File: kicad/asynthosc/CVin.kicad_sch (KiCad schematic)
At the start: 12 parts, among them J14 AudioJack3, SW11 SW_DIP_x04, U8 MCP6004

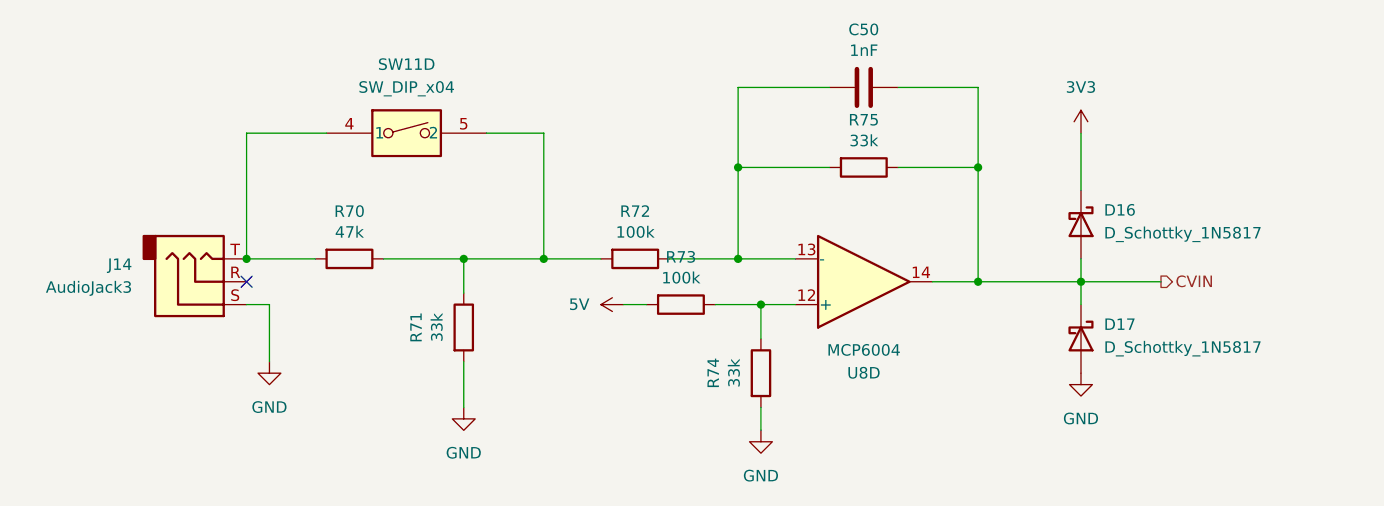
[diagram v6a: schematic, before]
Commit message: pcb: place and change some components for easier routing
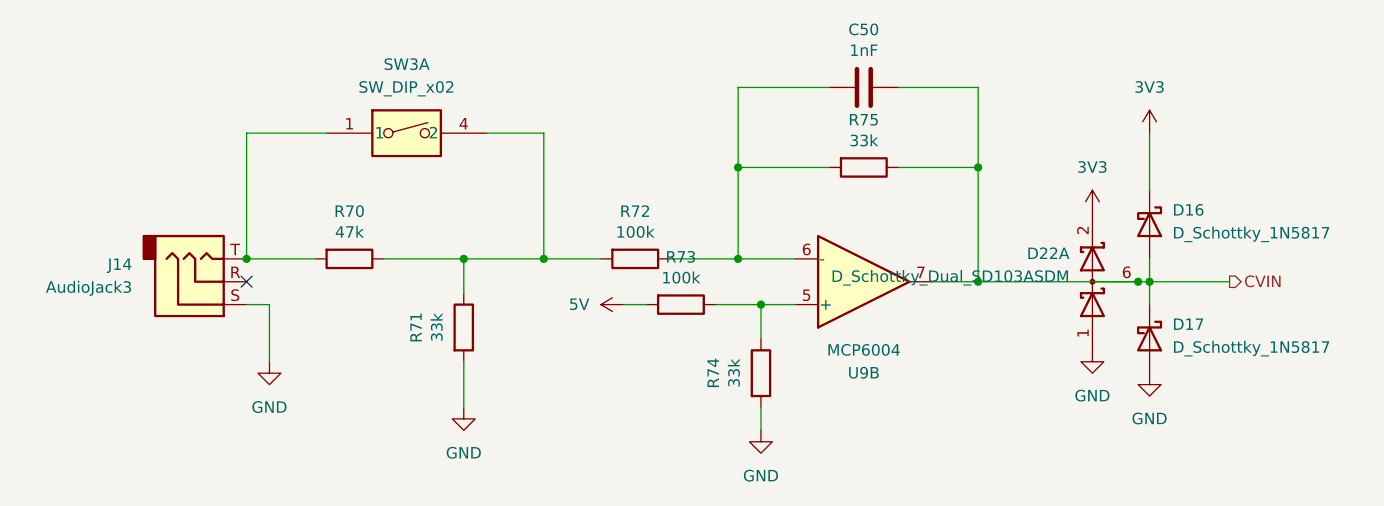
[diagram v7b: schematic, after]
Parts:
- removed SW11: SW_DIP_x04, Button_Switch_SMD:SW_DIP_SPSTx04_Slide_6.7x11.72mm_W8.61mm_P2.54mm_LowProfile, symbol asynthosc_lib:SW_DIP_x04_SEP
- added D22: D_Schottky_Dual_SD103ASDM, SOT-23-6, symbol asynthosc_lib:D_Schottky_Dual_SD103ASDM
- added SW3: SW_DIP_x02, Button_Switch_SMD:SW_DIP_SPSTx02_Slide_9.78x7.26mm_W8.61mm_P2.54mm, symbol asynthosc_lib:SW_DIP_x02_SEP
- renumbered U8 to U9
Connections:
- net 3V3: now also D22.2 (K)
- net CVIN: now also U9.7, D22.6 (common); no longer U9.14
- net GND: now also D22.1 (A)
- net at C50.2, R72.1, R75.2: now also U9.6 (-); no longer U9.13 (-)
- net at R70.1, R71.1, R72.2: now also SW3.4 (2)
- net at J14.T, R70.2: now also SW3.1
- net at R73.1, R74.1: now also U9.5 (+); no longer U9.12 (+)
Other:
- moved on the sheet: D16, D17

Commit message: pcb: place and draft route
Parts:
- removed D16, D17: D_Schottky_1N5817, Diode_SMD:D_SOD-123, symbol Device:D_Schottky
- renumbered D22 to D24, SW3 to SW4
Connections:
- net 3V3: now also D24.5 (K); no longer D24.2 (K)
- net CVIN: now also D24.3 (common); no longer D24.6 (common)
- net GND: now also D24.4 (A); no longer D24.1 (A)
- net at R70.1, R71.1, R72.2: now also SW4.3 (2); no longer SW4.4 (2)
- net at J14.T, R70.2: now also SW4.2 (1); no longer SW4.1
